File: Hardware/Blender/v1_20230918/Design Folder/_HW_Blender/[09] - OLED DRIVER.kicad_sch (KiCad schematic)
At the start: 6 parts, among them J901 RCPT_6POS_2.54MM_VERT

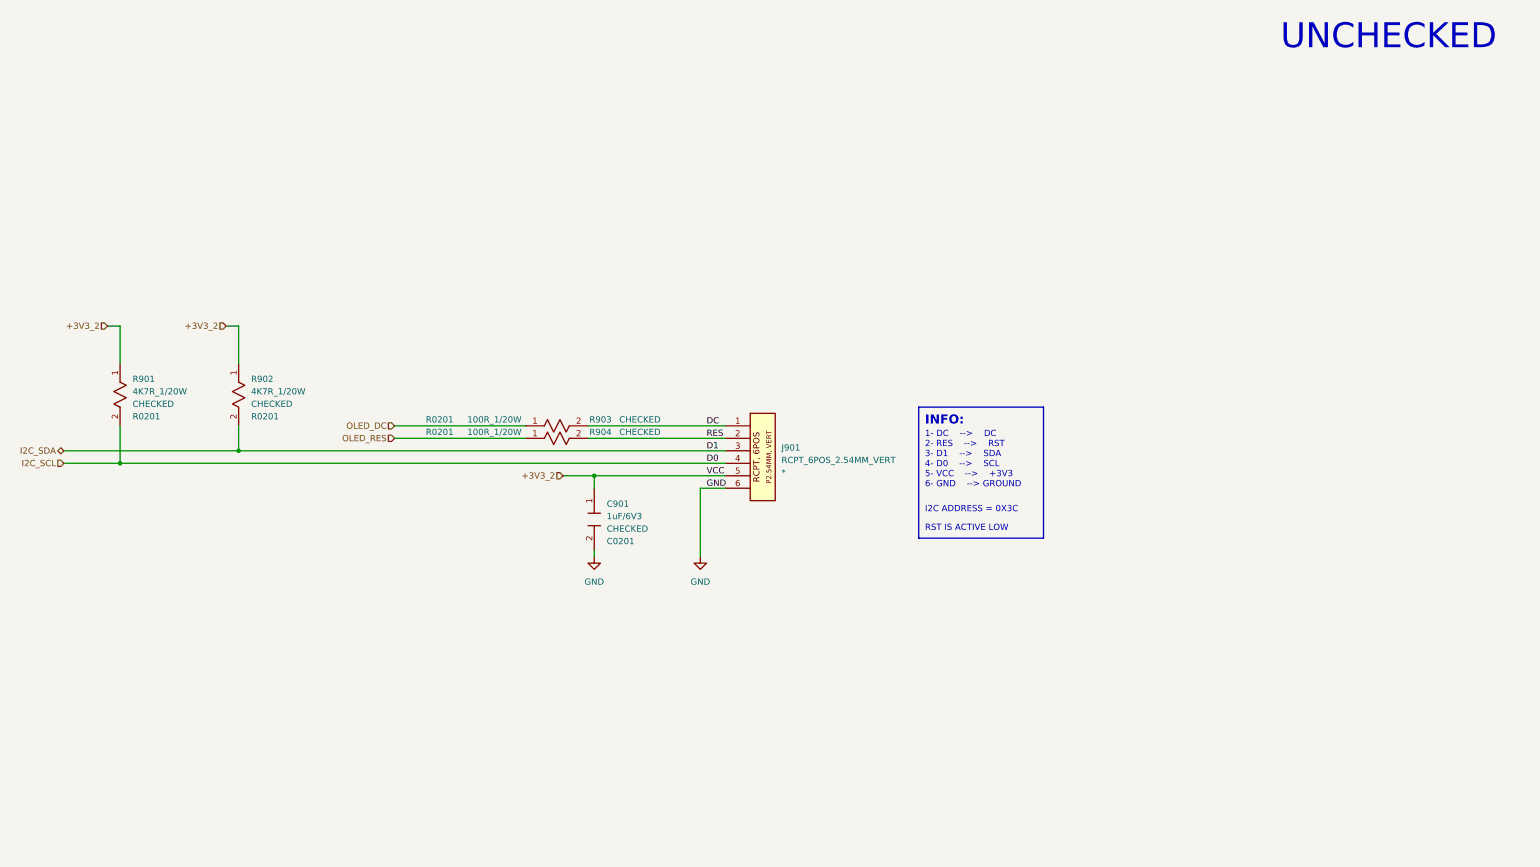
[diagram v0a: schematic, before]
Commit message: Improving the file structure and documentation
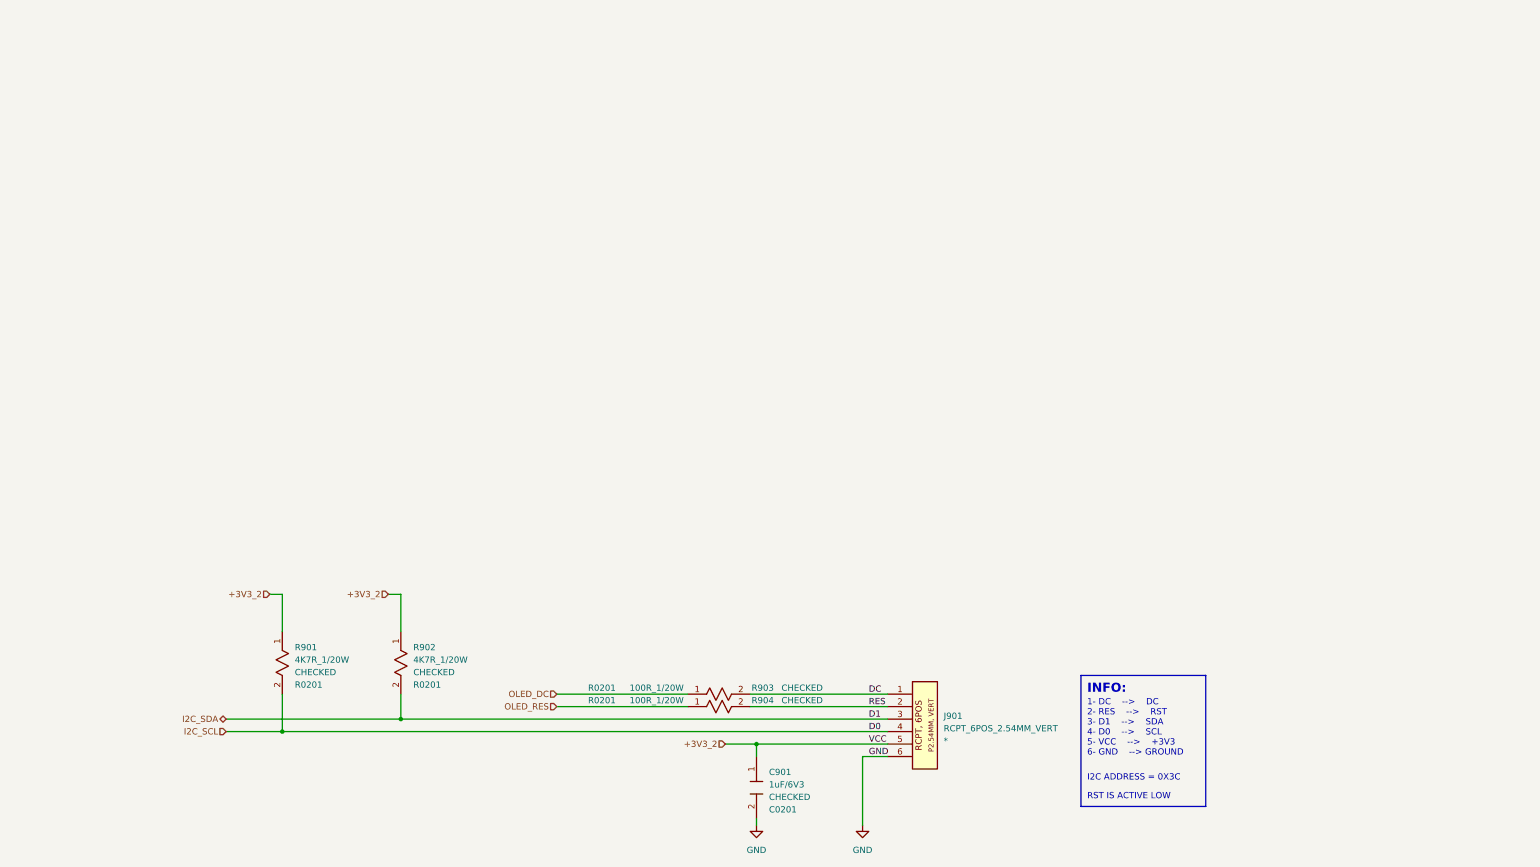
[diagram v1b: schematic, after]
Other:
- note removed: "UNCHECKED"
- moved on the sheet: C901, J901, R901, R902, R903, R904

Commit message: More update for hardware part
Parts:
- C901: value 1uF/6V3 -> 1uF_6V3_X5R; symbol _SCHLIB_Blender:CAP_1uF/6V3_C0201 -> _SCHLIB_Blender:CAP_1uF_6V3_X5R_C0201; Manufacturer (none) -> Samsung Electro-Mechanics; PCB CHECk (none) -> PCB (N/A); Part Number CL03A105MQ3CSNH -> (none); Part Number (Manufacturer) (none) -> CL03A105MQ3CSNH; Part Number (Vendor) (none) -> 1276-6441-2-ND; SCH CHECK CHECKED -> SCH (N/A); Vendor (none) -> Digikey
- J901: value RCPT_6POS_2.54MM_VERT -> RECEPT_6X1_VERT_2.54MM; symbol _SCHLIB_Blender:CONN_RCPT_6POS_2.54MM_VERT -> _SCHLIB_Blender:CONN_RECEPT_6POS_1ROW_VERT_2.54MM; Manufacturer (none) -> Sullins Connector Solutions; PCB CHECk (none) -> PCB (N/A); Package (none) -> THD-VERT-2.54MM; Part Number PPTC061LFBN-RC -> (none); Part Number (Manufacturer) (none) -> PPTC061LFBN-RC; Part Number (Vendor) (none) -> S7004-ND; SCH CHECK * -> SCH (N/A); Vendor (none) -> Digikey
- R901, R902: value 4K7R_1/20W -> 47KR_1/20W_1%; symbol _SCHLIB_Blender:RES_4K7R_1/20W-R0201 -> _SCHLIB_Blender:RES_47KR_1/20W_1%_R0201; Link https://www.digikey.ca/en/products/detail/stackpole-electro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 -> https://www.digikey.ca/en/products/detail/yageo/AC0201FR-07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; Manufacturer (none) -> YAGEO; PCB CHECk (none) -> PCB (N/A); Part Number RMCF0201FT4K70 -> (none); Part Number (Manufacturer) (none) -> AC0201FR-0747KL; Part Number (Vendor) (none) -> YAG3425TR-ND; SCH CHECK CHECKED -> SCH (N/A); Vendor (none) -> Digikey
- R903, R904: value 100R_1/20W -> 100R_1/20W_1%; symbol _SCHLIB_Blender:RES_100R_1/20W-R0201 -> _SCHLIB_Blender:RES_100R_1/20W_1%_R0201; Manufacturer (none) -> Stackpole Electronics Inc; PCB CHECk (none) -> PCB (N/A); Part Number RMCF0201FT100R -> (none); Part Number (Manufacturer) (none) -> RMCF0201FT100R; Part Number (Vendor) (none) -> RMCF0201FT100RTR-ND; SCH CHECK CHECKED -> SCH (N/A); Vendor (none) -> Digikey
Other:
- moved on the sheet: R903, R904
